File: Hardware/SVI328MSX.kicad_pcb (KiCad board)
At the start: 2 copper layers, 55 x 59 mm, 6 parts, among them J1 Conn_02x15_Odd_Even, J2 Conn_02x15_Odd_Even, U1 27C256, U2 74LS08

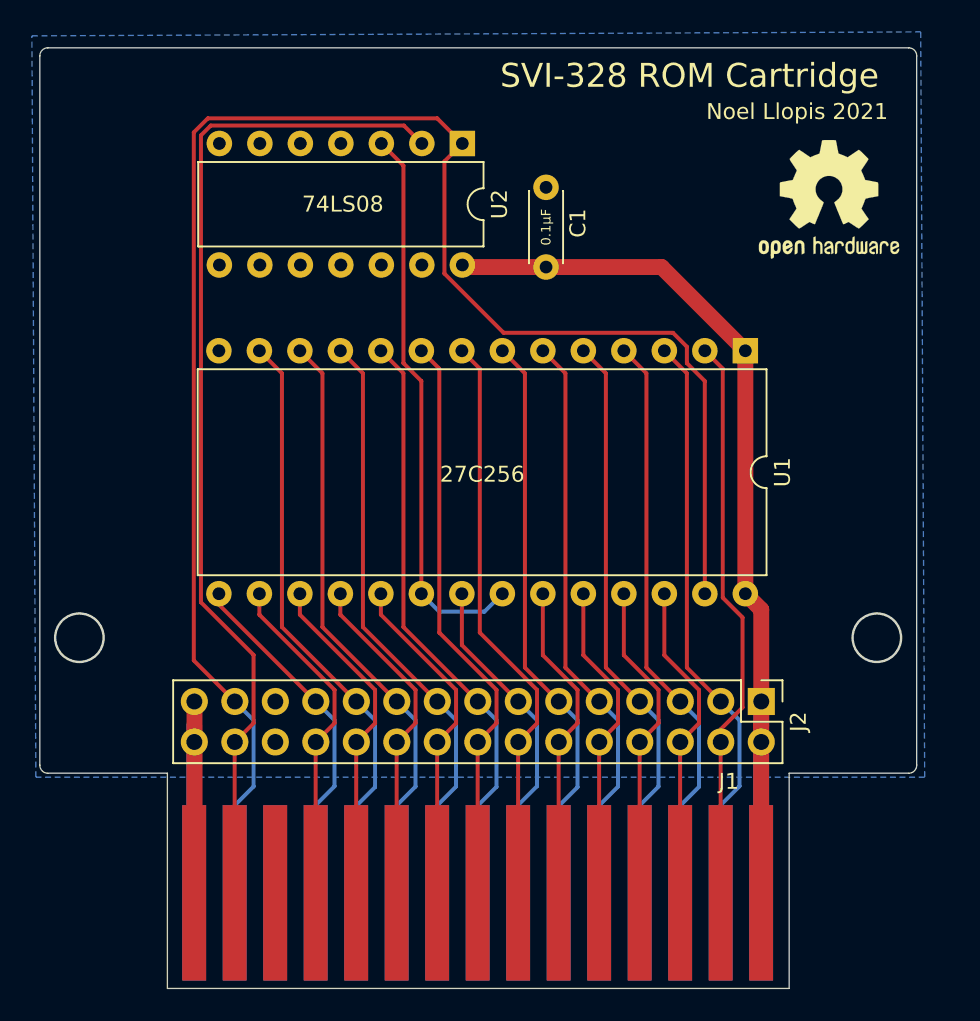
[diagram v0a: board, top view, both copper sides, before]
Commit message: Removed J1 and J2 labels
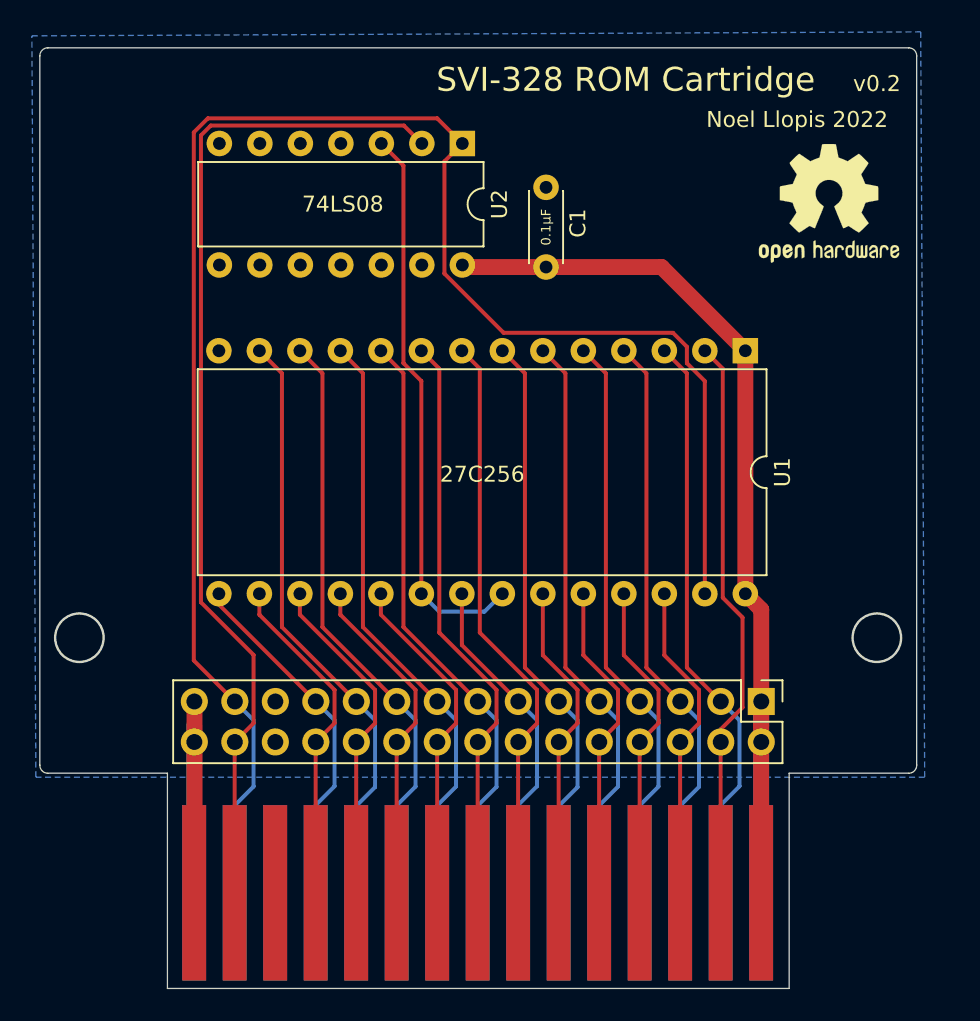
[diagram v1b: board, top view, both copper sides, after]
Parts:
- moved REF** 0.25 mm to (156.5, 54.8)
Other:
- board text added: "Noel Llopis 2022"
- board text added: "v0.2"
- board text removed: "Noel Llopis 2021"
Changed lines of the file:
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@@
     (at 134.46 98.127)
     (attr through_hole)
-    (fp_text reference "J1" (at 15.748 -7.112) (layer "F.SilkS")
+    (fp_text reference "J1" (at 15.748 -7.112) (layer "F.SilkS") hide
       (effects (font (size 1 1) (thickness 0.15)))
     )
@@
   )
   (footprint "Symbol:OSHW-Logo2_9.8x8mm_SilkScreen" (layer "F.Cu")
-    (at 156.5 54.5)
+    (at 156.5 54.75)
     (descr "Open Source Hardware Symbol")
     (tags "Logo Symbol OSHW")
@@
     (tags "Through hole pin header THT 2x15 2.54mm double row")
     (attr through_hole)
-    (fp_text reference "J2" (at 1.27 -2.33 90) (layer "F.SilkS")
+    (fp_text reference "J2" (at 1.27 -2.33 90) (layer "F.SilkS") hide
       (effects (font (size 1 1) (thickness 0.15)))
     )
@@
     (effects (font (size 1 1) (thickness 0.15)) (justify mirror))
   )
-  (gr_text "SVI-328 ROM Cartridge" (at 147.75 46.75) (layer "F.SilkS")
+  (gr_text "SVI-328 ROM Cartridge" (at 143.75 47) (layer "F.SilkS")
     (effects (font (size 1.5 1.5) (thickness 0.15)))
   )
-  (gr_text "Noel Llopis 2021" (at 154.5 49) (layer "F.SilkS")
+  (gr_text "Noel Llopis 2022" (at 154.5 49.5) (layer "F.SilkS")
     (effects (font (size 1 1) (thickness 0.15)))
   )
+  (gr_text "v0.2" (at 161 47.25) (layer "F.SilkS")
+    (effects (font (size 1 1) (thickness 0.15)) (justify right))
+  )
   (segment (start 129.804999 81.334999) (end 129.804999 65.414999) (width 0.25) (layer "F.Cu") (net 3))
